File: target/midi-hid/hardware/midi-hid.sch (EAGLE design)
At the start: 0 parts

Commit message: midi-hid hardware interim drop
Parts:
- added C1, C2: (no value), rcl:C-EUC0805
- added D1, D10, D11, D12, D13, D14, D15, D16, D17, D18, D19, D2, D20, D21, D22, D23, D24, D3, D4, D5, D6, D7, D8, D9: (no value), diode:DIODE-SOD80C
- added IC1: MEGA48/88/168-AU, avr-7:MEGA48/88/168-AU
- added PAD1, PAD10, PAD11, PAD12, PAD13, PAD14, PAD15, PAD16, PAD17, PAD18, PAD19, PAD2, PAD20, PAD21, PAD22, PAD23, PAD24, PAD25, PAD26, PAD27, PAD28, PAD29, PAD3, PAD30, PAD31, PAD32, PAD33, PAD34, PAD35, PAD36, PAD37, PAD38, PAD39, PAD4, PAD40, PAD41, PAD42, PAD43, PAD44, PAD45, PAD46, PAD47, PAD48, PAD49, PAD5, PAD50, PAD51, PAD52, PAD53, PAD54, PAD55, PAD56, PAD6, PAD7, PAD8, PAD9: (no value), wirepad:1,6/0,8
- added Q1: (no value), crystal:CRYSTALHC49S
- added R1, R10, R11, R12, R13, R14, R15, R16, R17, R18, R19, R2, R20, R21, R22, R23, R24, R25, R26, R27, R28, R29, R3, R30, R31, R32, R4, R5, R6, R7, R8, R9: (no value), rcl:R-EU_R0805
- added S1, S2, S3, S4: (no value), switch-omron:40-XX
- added SW1, SW2, SW3, SW4: EC12E_SW, switch-alps:EC12E_SW
- added T1, T2, T3, T4: (no value), transistor:MMBT3904LT1-NPN-SOT23-BEC
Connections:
- new net ADC6: IC1.ADC6
- new net ADC7: IC1.ADC7
- new net BUTROW0: IC1.PB3(MOSI/OC2A/PCINT3)
- new net BUTROW1: IC1.PB4(MISO/PCINT4)
- new net BUTROW2: IC1.PB5(SCK/PCINT5)
- new net COLUMN0: IC1.PC0(ADC0/PCINT8)
- new net COLUMN1: IC1.PC1(ADC1/PCINT9)
- new net COLUMN2: IC1.PC2(ADC2/PCINT10)
- new net COLUMN3: IC1.PC3(ADC3/PCINT11)
- new net ENCROWA: IC1.PB0(ICP1/CLKO/PCINT0)
- new net ENCROWB: IC1.PB1(OC1A/PCINT1)
- new net ENCROWS: IC1.PB2(SS/OC1B/PCINT2)
- new net GND: C1.2, C2.2, IC1.AGND, IC1.GND@1, IC1.GND@2, PAD11.P, PAD17.P, PAD23.P, PAD29.P, PAD35.P, PAD41.P, PAD47.P, PAD53.P
- new net INTOUT: IC1.PD1(TXD/PCINT17)
- new net LEDROW0: IC1.PD2(INT0/PCINT18)
- new net LEDROW1: IC1.PD3(INT1/OC2B/PCINT19)
- new net LEDROW2: IC1.PD4(T0/XCK/PCINT20)
- new net LEDROW3: IC1.PD5(T1/OC0B/PCINT21), R3.1
- new net LEDROW4: IC1.PD6(AIN0/OC0A/PCINT22)
- new net LEDROW5: IC1.PD7(AIN1/PCINT23)
- new net LEDROWB: IC1.PD0(RXD/PCINT16)
- new net N$10: SW2G$2.1
- new net N$11: D13.C, SW3G$1.B
- new net N$12: D14.C, SW3G$1.A
- new net N$14: D15.C, SW4G$1.B
- new net N$15: D16.C, SW4G$1.A
- new net N$17: SW4G$1.C
- new net N$18: SW4G$2.1
- new net N$19: SW3G$1.C
- new net N$20: SW3G$2.1
- new net N$21: C1.1, IC1.PB6(XTAL1/TOSC1/PCINT6), Q1.1
- new net N$22: C2.1, IC1.PB7(XTAL2/TOSC2/PCINT7), Q1.2
- new net N$23: R29.2, T1.B
- new net N$24: PAD36.P, R1.2
- new net N$25: PAD37.P, R2.2
- new net N$26: PAD38.P, R3.2
- new net N$27: R30.2, T2.B
- new net N$28: PAD42.P, R4.2
- new net N$29: PAD43.P, R5.2
- new net N$30: PAD44.P, R6.2
- new net N$31: R31.2, T3.B
- new net N$32: PAD48.P, R7.2
- new net N$33: PAD49.P, R8.2
- new net N$34: PAD50.P, R9.2
- new net N$35: R32.2, T4.B
- new net N$36: PAD54.P, R10.2
- new net N$37: PAD55.P, R11.2
- new net N$38: PAD56.P, R12.2
- new net N$39: PAD33.P
- new net N$4: SW1G$1.C
- new net N$40: D3.A, PAD34.P
- new net N$41: PAD39.P
- new net N$42: D7.A, PAD40.P
- new net N$43: PAD45.P
- new net N$44: D4.A, PAD46.P
- new net N$45: PAD51.P
- new net N$46: D8.A, PAD52.P
- new net N$47: PAD14.P, R15.2
- new net N$48: PAD13.P, R14.2
- new net N$49: PAD12.P, R13.2
- new net N$5: SW1G$2.1
- new net N$51: PAD20.P, R18.2
- new net N$52: PAD19.P, R17.2
- new net N$53: PAD18.P, R16.2
- new net N$54: R2.1
- new net N$55: R1.1
- new net N$56: PAD24.P, R19.2
- new net N$57: PAD25.P, R20.2
- new net N$58: PAD26.P, R21.2
- new net N$59: PAD32.P, R24.2
- new net N$6: D11.C, SW2G$1.B
- new net N$60: PAD31.P, R23.2
- new net N$61: PAD30.P, R22.2
- new net N$62: R7.1
- new net N$63: PAD9.P
- new net N$64: D1.A, PAD10.P
- new net N$65: PAD15.P
- new net N$66: D5.A, PAD16.P
- new net N$67: PAD21.P
- new net N$68: D2.A, PAD22.P
- new net N$69: PAD27.P
- new net N$7: D12.C, SW2G$1.A
- new net N$70: D6.A, PAD28.P
- new net N$71: PAD2.P
- new net N$72: PAD1.P, R28.2
- new net N$73: PAD4.P
- new net N$74: PAD3.P, R27.2
- new net N$75: PAD6.P
- new net N$76: PAD5.P, R26.2
- new net N$77: PAD8.P
- new net N$78: PAD7.P, R25.2
- new net N$79: R8.1
- new net N$80: R9.1
- new net N$81: R12.1
- new net N$82: R11.1
- new net N$83: R10.1
- new net N$84: R6.1
- new net N$85: R5.1
- new net N$86: R4.1
- new net N$9: SW2G$1.C
- new net RESET: IC1.PC6(/RESET/PCINT14)
- new net SCL: IC1.PC5(ADC5/SCL/PCINT13)
- new net SDA: IC1.PC4(ADC4/SDA/PCINT12)
- new net VCC: IC1.AREF, IC1.AVCC, IC1.VCC@1, IC1.VCC@2

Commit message: midi-hid hardware interim drop
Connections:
- new net C0: D1.C, D3.C, SW1G$1.C, SW1G$2.1, T1.C
- new net C1: D5.C, D7.C, SW2G$1.C, SW2G$2.1, T2.C
- new net C2: D2.C, D4.C, SW3G$1.C, SW3G$2.1, T3.C
- new net C3: D6.C, D8.C, SW4G$1.C, SW4G$2.1, T4.C
- new net N$1: D9.C, SW1G$1.B
- new net N$13: D19.C, SW3G$2.2
- new net N$16: D20.C, SW4G$2.2
- new net N$2: D10.C, SW1G$1.A
- new net N$3: D17.C, SW1G$2.2
- new net N$50: R24.1
- new net N$8: D18.C, SW2G$2.2
- new net N$87: R16.1
- new net N$91: R31.1
- new net N$95: R32.1
- net COLUMN0: now also R29.1
- net COLUMN1: now also R30.1
- net ENCROWA: now also D10.A, D12.A, D14.A, D16.A
- net ENCROWB: now also D11.A, D13.A, D15.A, D9.A
- net ENCROWS: now also D17.A, D18.A, D19.A, D20.A
- net GND: now also T1.E, T2.E, T3.E, T4.E
- net LEDROW4: now also R2.1
- net LEDROW5: now also R1.1
- net N$10: now also R19.1; no longer SW2G$2.1
- net N$17: now also R20.1; no longer SW4G$1.C
- net N$18: now also R21.1; no longer SW4G$2.1
- net N$19: now also R22.1; no longer SW3G$1.C
- net N$20: now also R23.1; no longer SW3G$2.1
- net N$4: now also R13.1; no longer SW1G$1.C
- net N$5: now also R14.1; no longer SW1G$2.1
- net N$54: now also R18.1; no longer R2.1
- net N$55: now also R17.1; no longer R1.1
- net N$9: now also R15.1; no longer SW2G$1.C
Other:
- moved on the sheet: D1, D11, D12, D13, D14, D15, D16, D18, D19, D2, D20, D22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

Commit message: routing midi-hid
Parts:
- added C3, C4: (no value), rcl:C-EUC0805
- added C5: (no value), rcl:CPOL-EUE2.5-6
- added PAD57, PAD58, PAD59: WIREPAD1,6/0,8, wirepad:WIREPAD1,6/0,8
- added R33, R34: (no value), rcl:R-EU_0207/10
- added SV1: (no value), con-lstb:MA05-1
- added USBCONN: MICRO-USB, microusb:MICRO-USB
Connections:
- removed net N$10: R19.1
- removed net N$17: R20.1
- removed net N$18: R21.1
- removed net N$19: R22.1
- removed net N$20: R23.1
- removed net N$39: PAD33.P
- removed net N$4: R13.1
- removed net N$41: PAD39.P
- removed net N$43: PAD45.P
- removed net N$45: PAD51.P
- removed net N$5: R14.1
- removed net N$50: R24.1
- removed net N$54: R18.1
- removed net N$55: R17.1
- removed net N$62: R7.1
- removed net N$63: PAD9.P
- removed net N$65: PAD15.P
- removed net N$67: PAD21.P
- removed net N$69: PAD27.P
- removed net N$71: PAD2.P
- removed net N$73: PAD4.P
- removed net N$75: PAD6.P
- removed net N$77: PAD8.P
- removed net N$79: R8.1
- removed net N$80: R9.1
- removed net N$81: R12.1
- removed net N$82: R11.1
- removed net N$83: R10.1
- removed net N$84: R6.1
- removed net N$85: R5.1
- removed net N$86: R4.1
- removed net N$87: R16.1
- removed net N$9: R15.1
- removed net N$95: R32.1
- new net DM: USBCONN.D-
- new net DP: USBCONN.D+
- new net ID: USBCONN.ID
- new net N$88: D22.C, S2.S1
- new net N$89: D21.C, S1.S1
- new net N$90: D23.C, S3.S1
- net ADC6: now also PAD58.P
- net ADC7: now also PAD59.P
- net BUTROW0: now also PAD33.P, PAD39.P, PAD45.P, PAD51.P
- net BUTROW1: now also PAD15.P, PAD21.P, PAD27.P, PAD9.P
- net BUTROW2: now also D21.A, D22.A, D23.A, D24.A
- net C0: now also PAD2.P, S1.P1
- net C1: now also PAD4.P, S2.P1
- net C2: now also PAD6.P, S3.P1
- net C3: now also PAD8.P, S4.P1
- net COLUMN2: now also R31.1
- net COLUMN3: now also R32.1
- net GND: now also C3.2, C4.2, C5.-, SV1.2, USBCONN.GND
- net INTOUT: now also SV1.5
- net LEDROW0: now also R15.1, R18.1, R21.1, R24.1
- net LEDROW1: now also R14.1, R17.1, R20.1, R23.1
- net LEDROW2: now also R13.1, R16.1, R19.1, R22.1
- net LEDROW3: now also R12.1, R6.1, R9.1
- net LEDROW4: now also R11.1, R5.1, R8.1
- net LEDROW5: now also R10.1, R4.1, R7.1
- net LEDROWB: now also R25.1, R26.1, R27.1, R28.1
- net N$91: now also D24.C, S4.S1; no longer R31.1
- net RESET: now also PAD57.P
- net SCL: now also SV1.3
- net SDA: now also SV1.4
- net VCC: now also C3.1, C4.1, C5.+, SV1.1, USBCONN.VCC
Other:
- moved on the sheet: C1, C2, D1, D11, D12, D15, D16, D18, D2, D20, D21, D22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

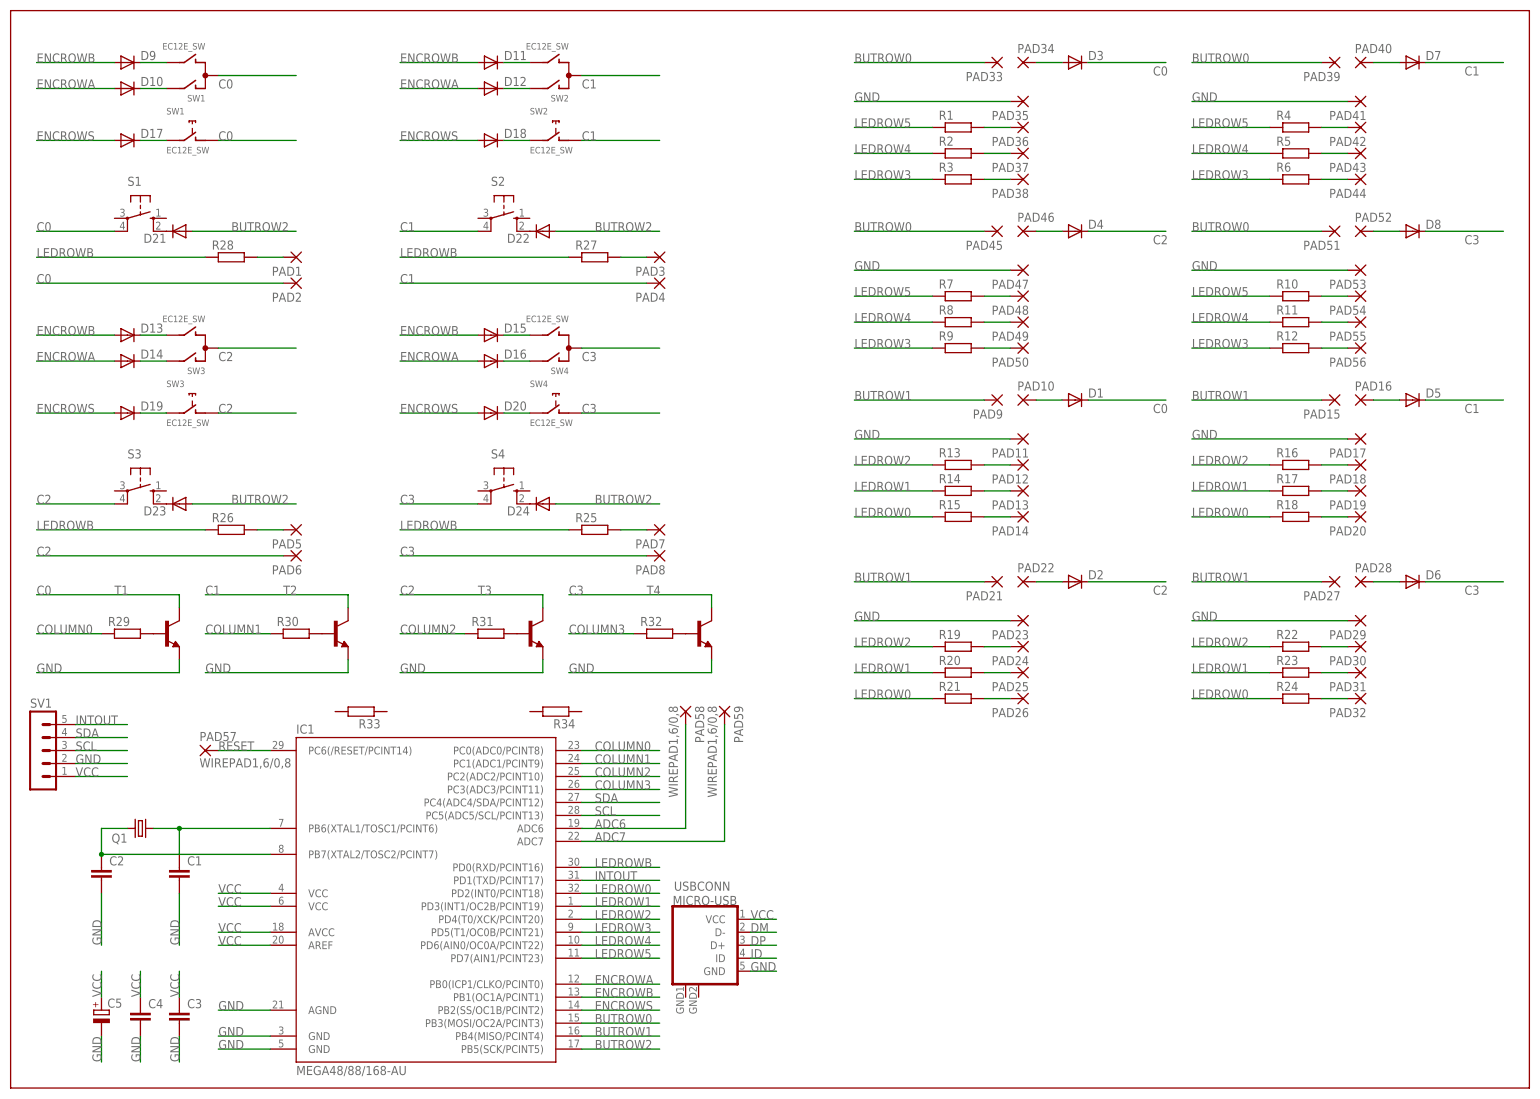
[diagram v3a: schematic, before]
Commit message: midi-hid hardware
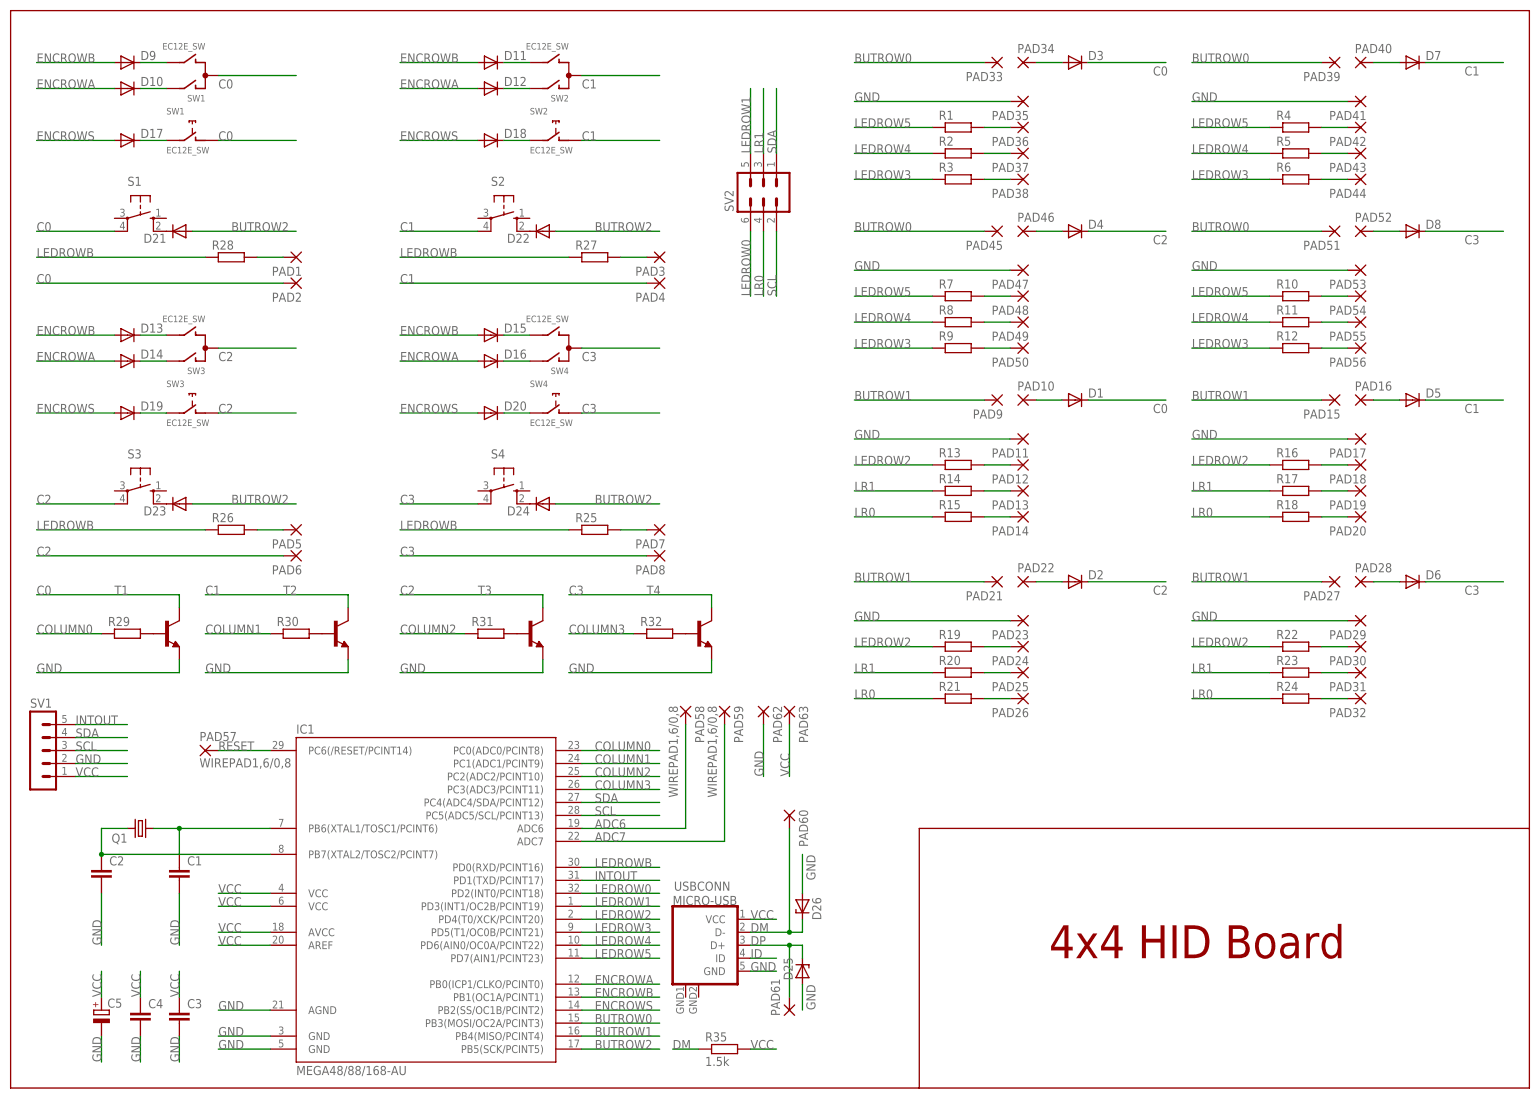
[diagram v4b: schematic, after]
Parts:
- removed R33, R34: (no value), rcl:R-EU_0207/10
- added D25, D26: (no value), diode:ZENER-DIODESOD80C
- added PAD60, PAD61, PAD62, PAD63: (no value), wirepad:1,6/0,8
- added R35: 1.5k, rcl:R-EU_R0805
- added SV2: (no value), con-lstb:MA03-2
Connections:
- new net LR0: R15.1, R18.1, R21.1, R24.1, SV2.4
- new net LR1: R14.1, R17.1, R20.1, R23.1, SV2.3
- net DM: now also D26.C, PAD60.P, R35.1
- net DP: now also D25.C, PAD61.P
- net GND: now also D25.A, D26.A, PAD62.P
- net LEDROW0: now also SV2.6; no longer R15.1, R18.1, R21.1, R24.1
- net LEDROW1: now also SV2.5; no longer R14.1, R17.1, R20.1, R23.1
- net SCL: now also SV2.2
- net SDA: now also SV2.1
- net VCC: now also PAD63.P, R35.2
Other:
- note added: "4x4 HID Board"
